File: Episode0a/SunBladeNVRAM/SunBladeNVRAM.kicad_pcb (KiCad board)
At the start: 2 copper layers, 36.5 x 18.5 mm, 10 parts, among them J1 Conn_01x14_Pin, J2 Conn_01x14_Pin, J3 Conn_01x02_Pin, J4 Conn_01x02_Pin, J5 Conn_01x01_Pin, J6 Conn_01x01_Pin, J7 Conn_01x01_Pin, J8 Conn_01x01_Pin, U1 M48T59Y-70MH1, Y1 32.768 kHz

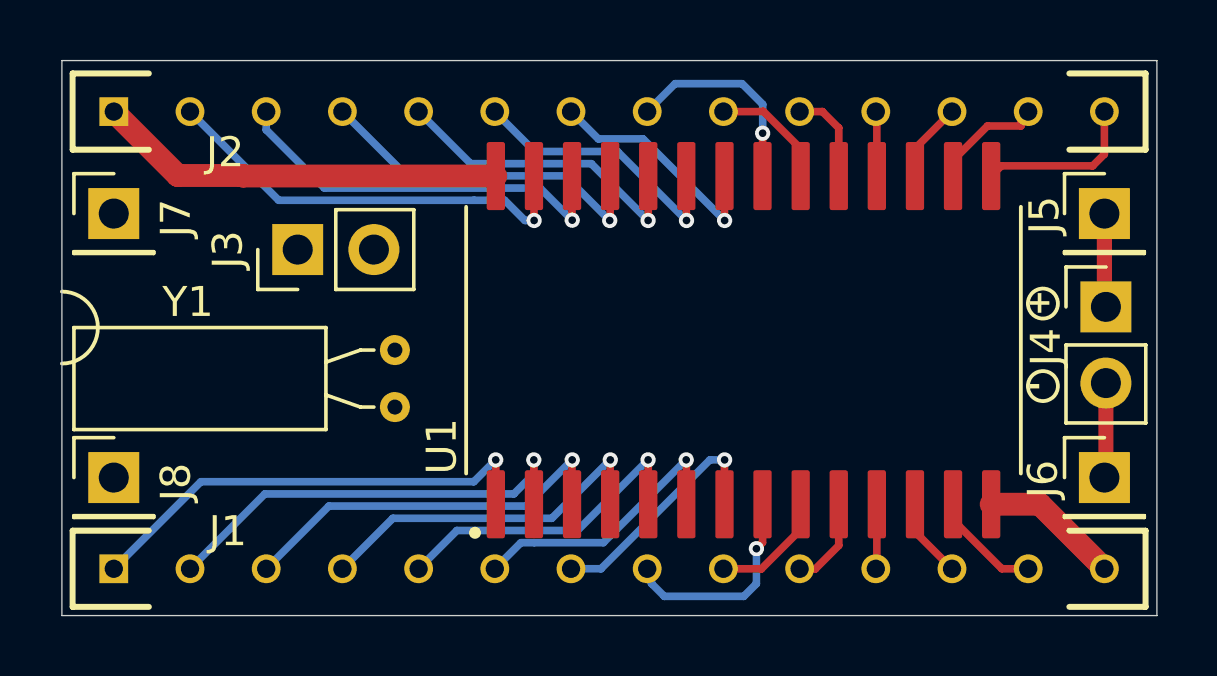
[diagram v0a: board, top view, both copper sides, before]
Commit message: remove xtal from bottom PCB
There's no point in wiring the xtal to the bottom PCB
since it can be soldered directly to the snap connectors
on the M48T59Y-70MH1.

Also, increase the size of the "notch" arc on the bottom
PCB, and add it to the top PCB.
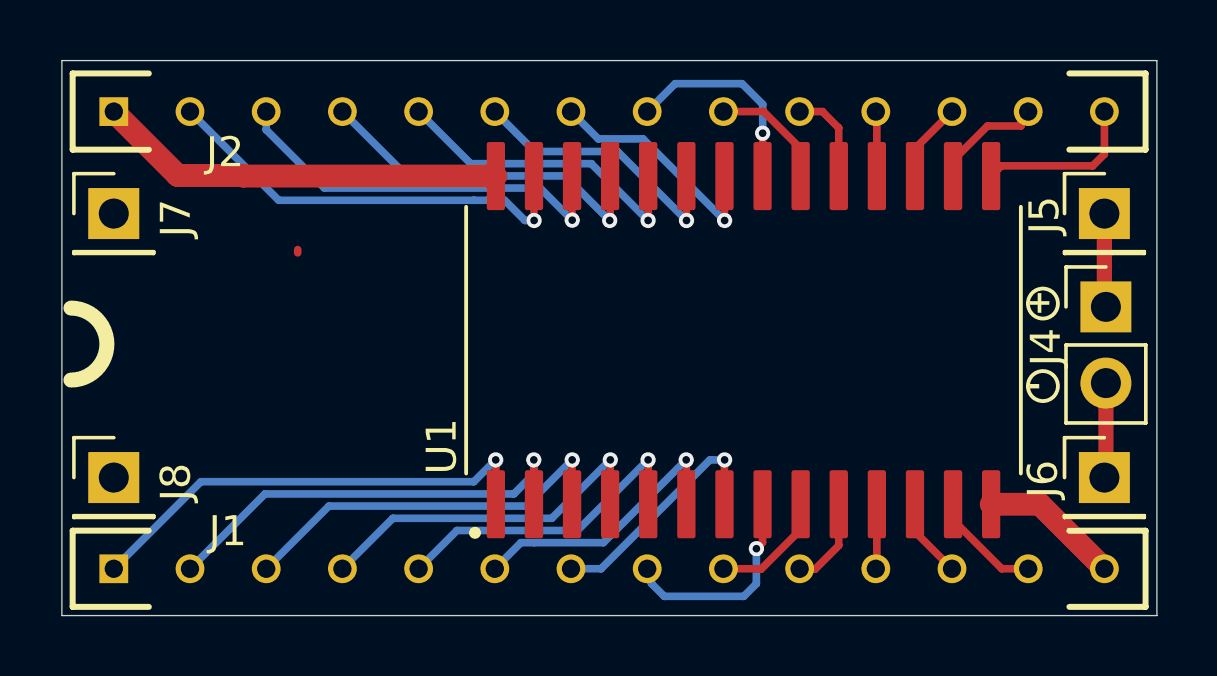
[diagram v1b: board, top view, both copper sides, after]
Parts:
- removed J3: Conn_01x02_Pin, Connector_PinHeader_2.54mm:PinHeader_1x02_P2.54mm_Vertical
- removed Y1: 32.768 kHz, Crystal:Crystal_C38-LF_D3.0mm_L8.0mm_Horizontal
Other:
- board text added: "Sun Blade 150 NVRAM replacement (c) 2024, daveho hacks https://github.com/daveho/SunBladeNVRAM Revision 3, 6-Jan-2025"
- board text removed: "Sun Blade 150 NVRAM replacement (c) 2024, daveho hacks https://github.com/daveho/SunBladeNVRAM Revision 2, 10-Dec-2024"
